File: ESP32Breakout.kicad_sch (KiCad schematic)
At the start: 18 parts, among them J1 PIN10-13_Breakout, J3 USB_C_Receptacle_USB2.0_16P, SW1 PTS636SM43SMTR LFS, SW2 PTS636SM43SMTR LFS, U1 ESP32-S3-WROOM-1U

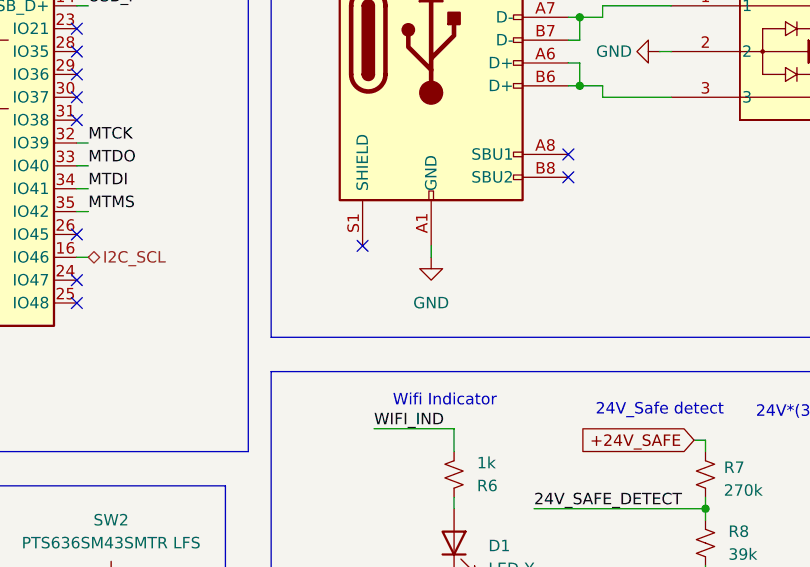
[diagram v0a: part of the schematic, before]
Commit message: grounded usb-c receptacle shield
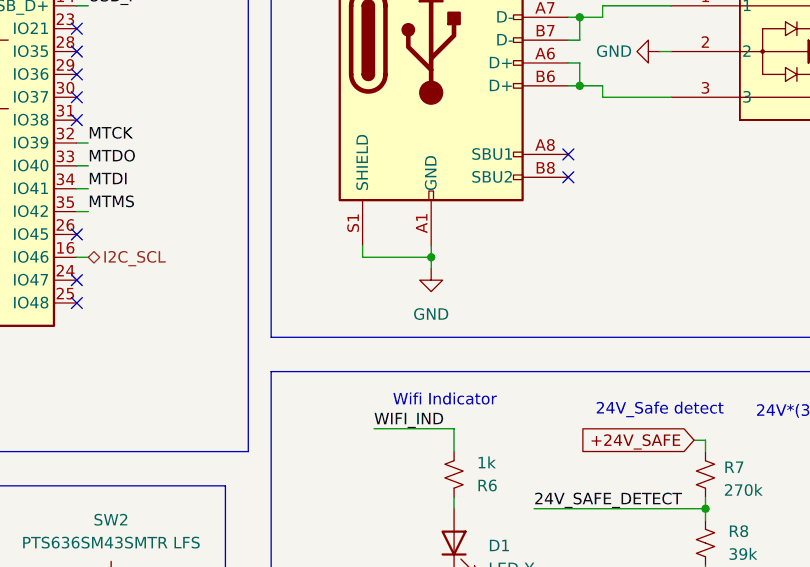
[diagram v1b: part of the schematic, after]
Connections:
- net GND: now also J3.S1 (SHIELD)
- no-connect marks 16 -> 15
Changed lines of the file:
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@@
+	)
+	(junction
+		(at 158.75 93.98)
+		(diameter 0)
+		(color 0 0 0 0)
 	)
 	(junction
@@
 	)
 	(no_connect
-		(at 151.13 92.71)
-	)
-	(no_connect
 		(at 119.38 68.58)
 	)
@@
 	(wire
 		(pts
+			(xy 151.13 93.98) (xy 158.75 93.98)
+		)
+		(stroke
+			(width 0)
+			(type default)
+		)
+	)
+	(wire
+		(pts
 			(xy 173.99 59.69) (xy 175.26 59.69)
 		)
@@
 	(wire
 		(pts
+			(xy 158.75 93.98) (xy 158.75 95.25)
+		)
+		(stroke
+			(width 0)
+			(type default)
+		)
+	)
+	(wire
+		(pts
 			(xy 76.2 53.34) (xy 88.9 53.34)
 		)
@@
 		(pts
 			(xy 113.03 130.81) (xy 118.11 130.81)
+		)
+		(stroke
+			(width 0)
+			(type default)
+		)
+	)
+	(wire
+		(pts
+			(xy 151.13 92.71) (xy 151.13 93.98)
 		)
 		(stroke
@@
 	(symbol
 		(lib_id "power:GND")
-		(at 158.75 93.98 0)
+		(at 158.75 95.25 0)
 		(unit 1)
 		(exclude_from_sim no)
@@
 		(fields_autoplaced yes)
 		(property "Reference" "#PWR014"
+			(at 158.75 101.6 0)
+			(effects
+				(font
+					(size 1.27 1.27)
+				)
+				(hide yes)
+			)
+		)
+		(property "Value" "GND"
 			(at 158.75 100.33 0)
 			(effects
@@
 					(size 1.27 1.27)
 				)
-				(hide yes)
-			)
-		)
-		(property "Value" "GND"
-			(at 158.75 99.06 0)
-			(effects
-				(font
-					(size 1.27 1.27)
-				)
 			)
 		)
 		(property "Footprint" ""
-			(at 158.75 93.98 0)
+			(at 158.75 95.25 0)
 			(effects
 				(font
@@
 		)
 		(property "Datasheet" ""
-			(at 158.75 93.98 0)
+			(at 158.75 95.25 0)
 			(effects
 				(font
@@
 		)
 		(property "Description" "Power symbol creates a global label with name \"GND\" , ground"
-			(at 158.75 93.98 0)
-			(effects
-				(font
+			(at 158.75 95.25 0)
+			(effects
+				(font

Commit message: minor fixes
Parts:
- U1: footprint RF_Module:ESP32-S3-WROOM-1 -> RF_Module:ESP32-S3-WROOM-1U
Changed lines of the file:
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@@
 			)
 		)
-		(property "Footprint" "RF_Module:ESP32-S3-WROOM-1"
+		(property "Footprint" "RF_Module:ESP32-S3-WROOM-1U"
 			(at 104.14 73.66 0)
 			(effects

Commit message: add 2 stage lockout to ignitor, add ignitor resistance reading with adc current source
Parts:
- renumbered C1 to C12, C3 to C13, C4 to C14, C2 to C15, C5 to C16, D1 to D8, J3 to J4, J1 to J5, R1 to R27, R6 to R28, R4 to R29, R5 to R30, R7 to R31, R8 to R32, U1 to U6
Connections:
- net 24V_SAFE_DETECT: now also U6.15 (IO3); no longer U6.6 (IO6)
- net I2C_SCL: now also U6.26 (IO45); no longer U6.16 (IO46)
- net I2C_SDA: now also U6.25 (IO48); no longer U6.15 (IO3)
- net IGNITOR_CTL renamed IGNITOR_PRIME_CTL
- new net IGNITOR_RUN_CTL: U6.6 (IO6)
- no-connect marks 15 -> 14

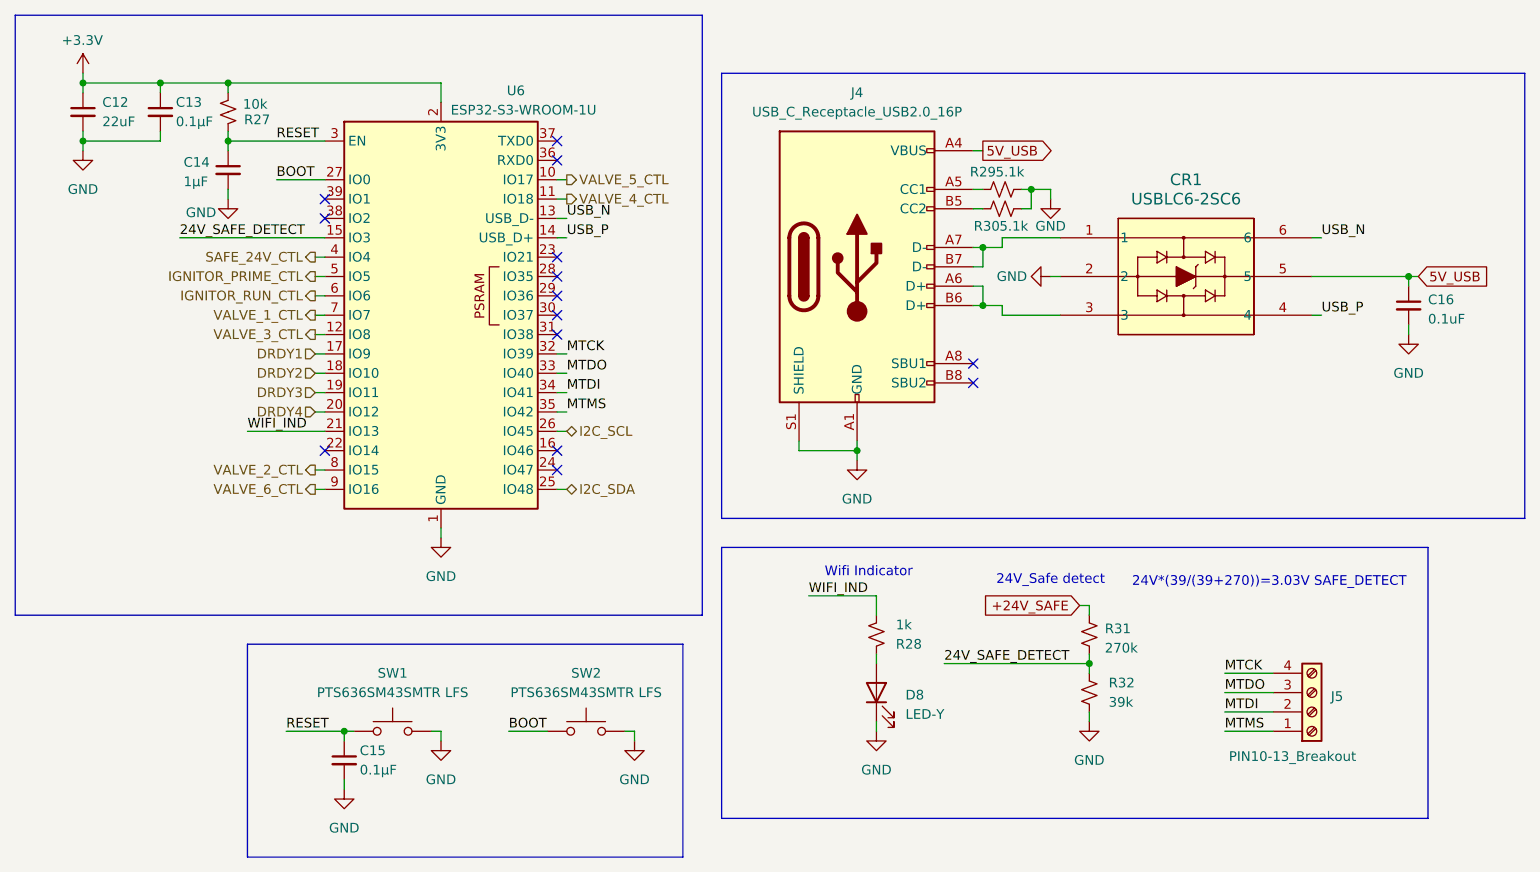
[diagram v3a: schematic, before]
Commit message: ground floating trace between ign relays when relays open
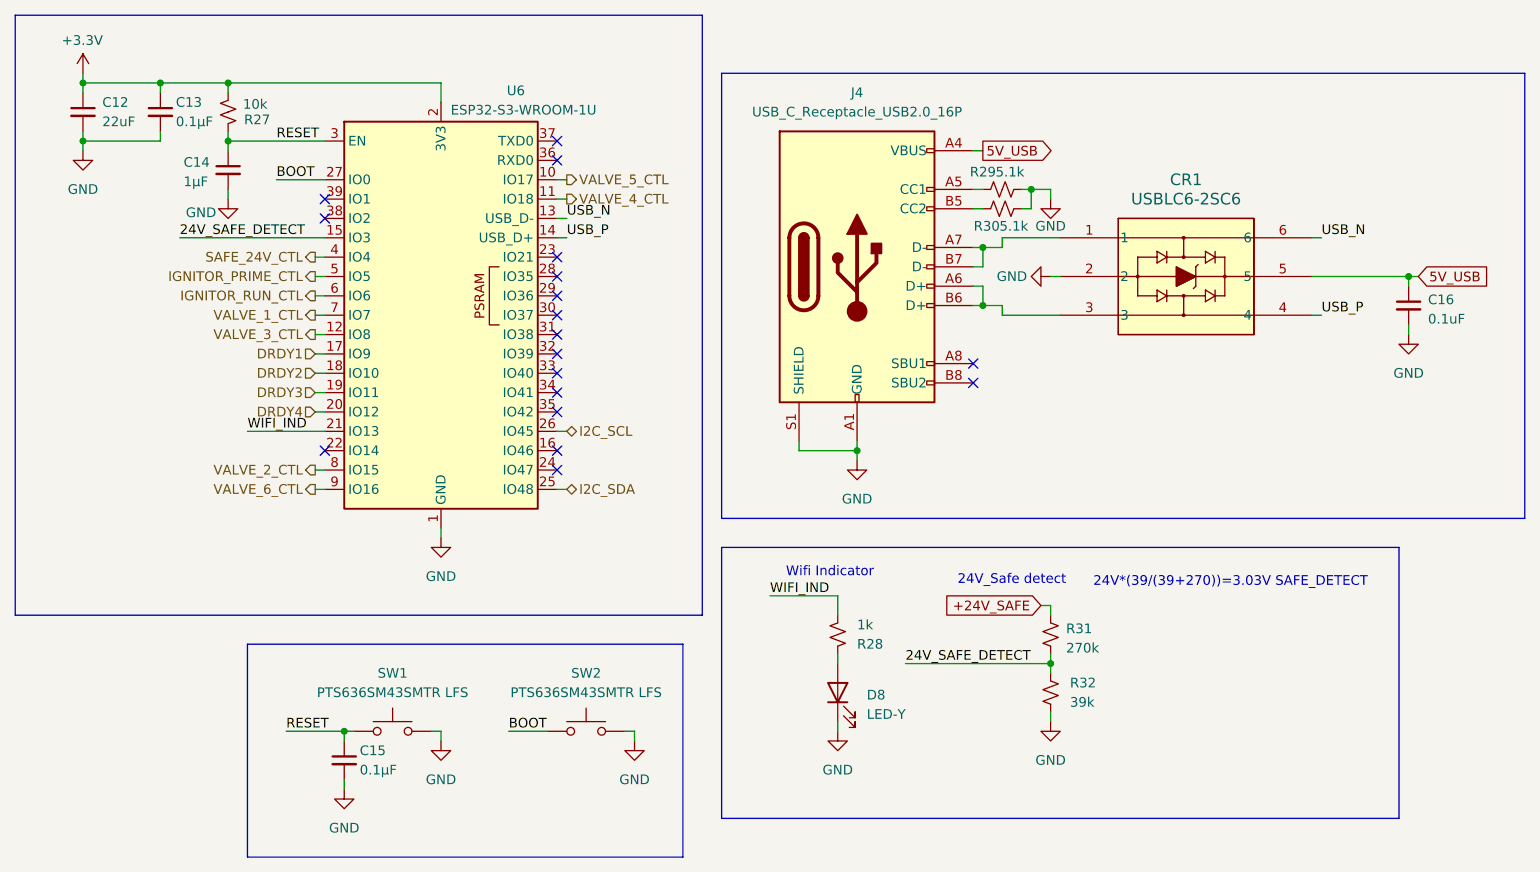
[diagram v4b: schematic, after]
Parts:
- removed J5: PIN10-13_Breakout, TerminalBlock:TerminalBlock_Xinya_XY308-2.54-4P_1x04_P2.54mm_Horizontal, symbol Connector:Screw_Terminal_01x04
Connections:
- net MTCK: no longer names the net of U6.32 (IO39)
- net MTDI: no longer names the net of U6.34 (IO41)
- net MTDO: no longer names the net of U6.33 (IO40)
- net MTMS: no longer names the net of U6.35 (IO42)
- no-connect marks 14 -> 18
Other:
- moved on the sheet: D8, R28, R31, R32
